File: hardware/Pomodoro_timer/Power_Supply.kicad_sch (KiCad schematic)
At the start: 17 parts, among them J1 USB_C_Receptacle_USB2.0_16P, J2 Battery_Terminals, Q1 FS8205A, U1 TP4056-42-ESOP8, U2 DW01A, U3 AP2127K-3.3

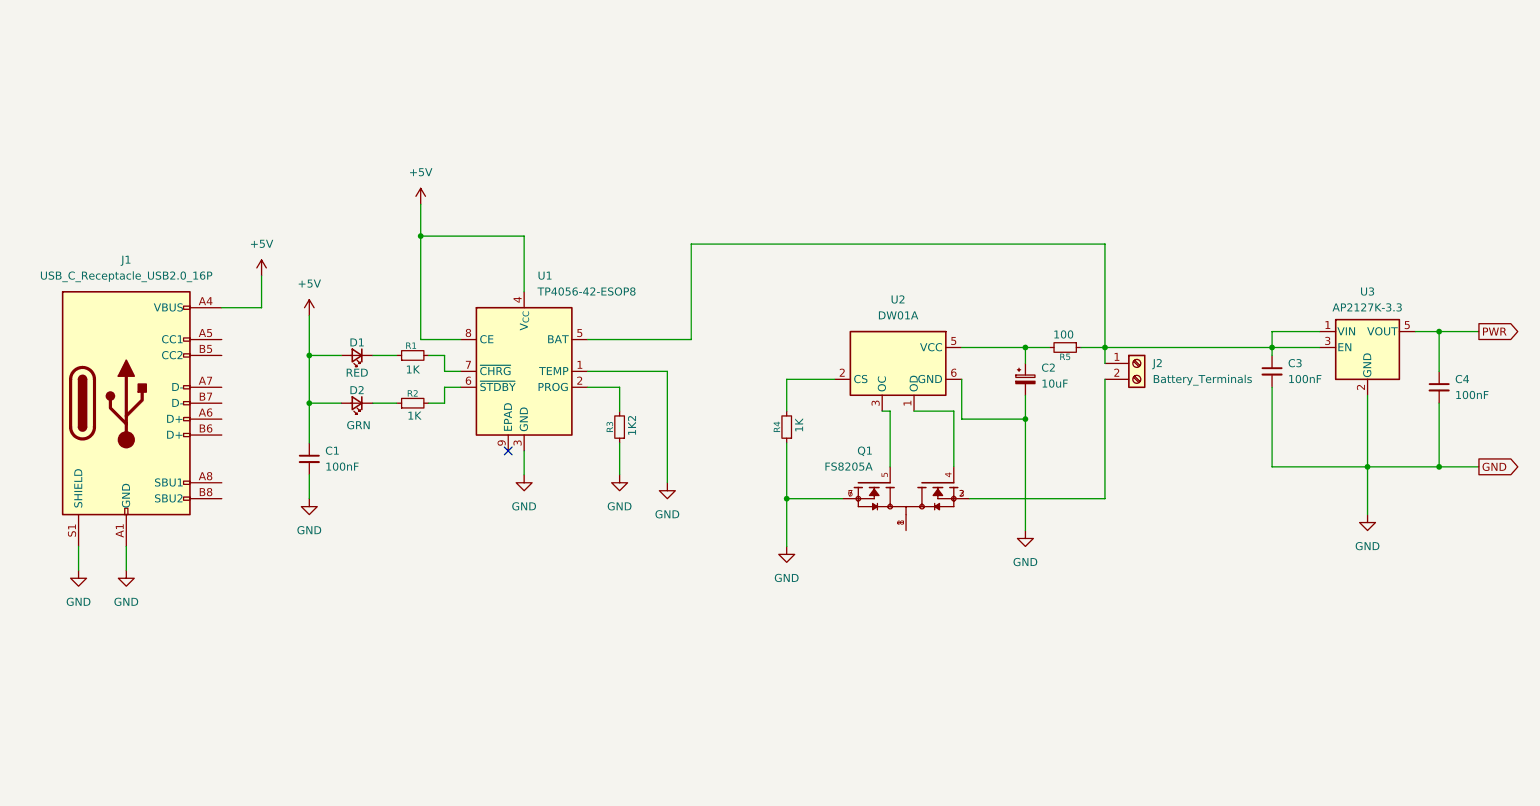
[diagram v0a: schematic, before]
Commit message: TM1637 Design started
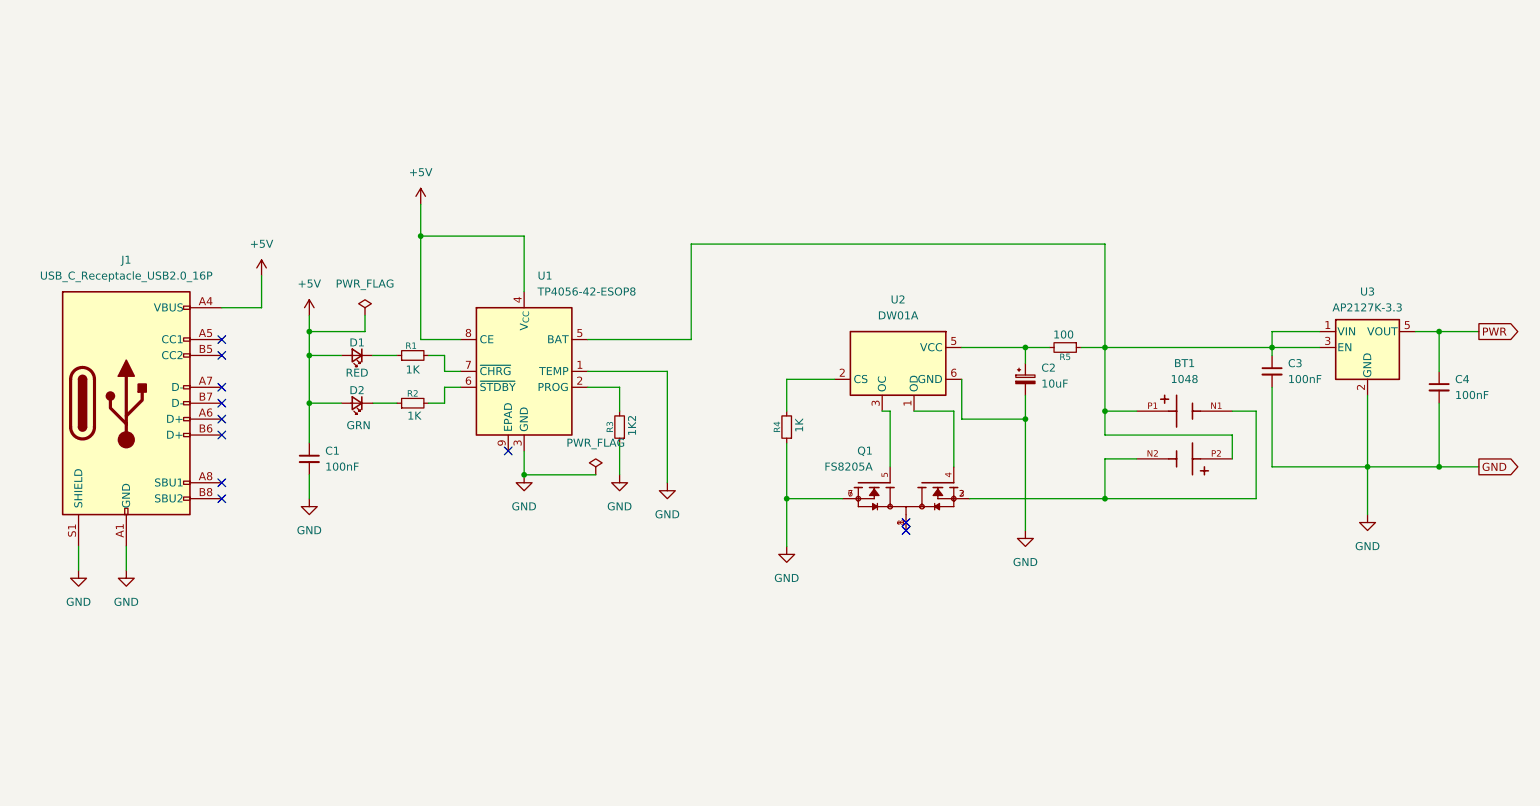
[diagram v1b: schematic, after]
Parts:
- removed J2: Battery_Terminals, symbol Connector:Screw_Terminal_01x02
- added BT1: 1048, 1048:BAT_1048, symbol 1048:1048
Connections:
- net at C3.1, R5.1, U1.5 (BAT)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: now also BT1.P1, BT1.P2
- net at Q1.2, Q1.3: now also BT1.N1, BT1.N2
- no-connect marks 1 -> 11

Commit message: PCB Ver.A : The Schematic completed the next part for PCB can be started.
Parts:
- removed BT1: 1048, 1048:BAT_1048, symbol 1048:1048
- removed C2: 10uF, symbol Device:C_Polarized_Small
- removed C3, C4: 100nF, symbol Device:C_Small
- removed D1: RED, symbol Device:LED_Small
- removed D2: GRN, symbol Device:LED_Small
- removed J1: USB_C_Receptacle_USB2.0_16P, symbol Connector:USB_C_Receptacle_USB2.0_16P
- removed Q1: FS8205A, FS8205A:SOP65P640X120-8N, symbol FS8205A:FS8205A
- removed R2, R4: 1K, symbol Device:R_Small
- removed R5: 100, symbol Device:R_Small
- removed U1: TP4056-42-ESOP8, Package_SO:SOIC-8-1EP_3.9x4.9mm_P1.27mm_EP2.41x3.3mm_ThermalVias, symbol Battery_Management:TP4056-42-ESOP8
- removed U2: DW01A, Package_TO_SOT_SMD:SOT-23-6, symbol Battery_Management:DW01A
- removed U3: AP2127K-3.3, Package_TO_SOT_SMD:SOT-223-3_TabPin2, symbol Regulator_Linear:AP2127K-3.3
- added BZ1: Buzzer, symbol Device:Buzzer
- added J1: Debug_Conn, symbol Connector:Conn_01x04_Pin
- added Q1: BC547, Package_TO_SOT_THT:TO-92, symbol Transistor_BJT:BC547
- added SW1: SW_Push, symbol Switch:SW_Push
- added U1: STM32G070CBTx, Package_QFP:LQFP-48_7x7mm_P0.5mm, symbol MCU_ST_STM32G0:STM32G070CBTx
- R3: value 1K2 -> 1K
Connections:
- net +5V is gone; now on net PWR: C1.1
- net GND: now also J1.1 (Pin_1), Q1.3 (E), SW1.1, U1.7 (VSS); no longer R3.1
- net PWR: now also R1.1, BZ1.1 (+), J1.4 (Pin_4), U1.4 (VBAT), U1.5 (VREF+), U1.6 (VDD)
- net at R3.2: now also Q1.2 (B)
- net at R1.2: now also SW1.2, U1.10 (NRST)
- new net: R3.1, U1.47 (PB8)
- new net: J1.2 (Pin_2), U1.36 (PA14)
- new net: J1.3 (Pin_3), U1.35 (PA13)
- new net: BZ1.2 (-), Q1.1 (C)
- new net CLK: U1.26 (PB14)
- new net DIO: U1.27 (PB15)
- no-connect marks 11 -> 0

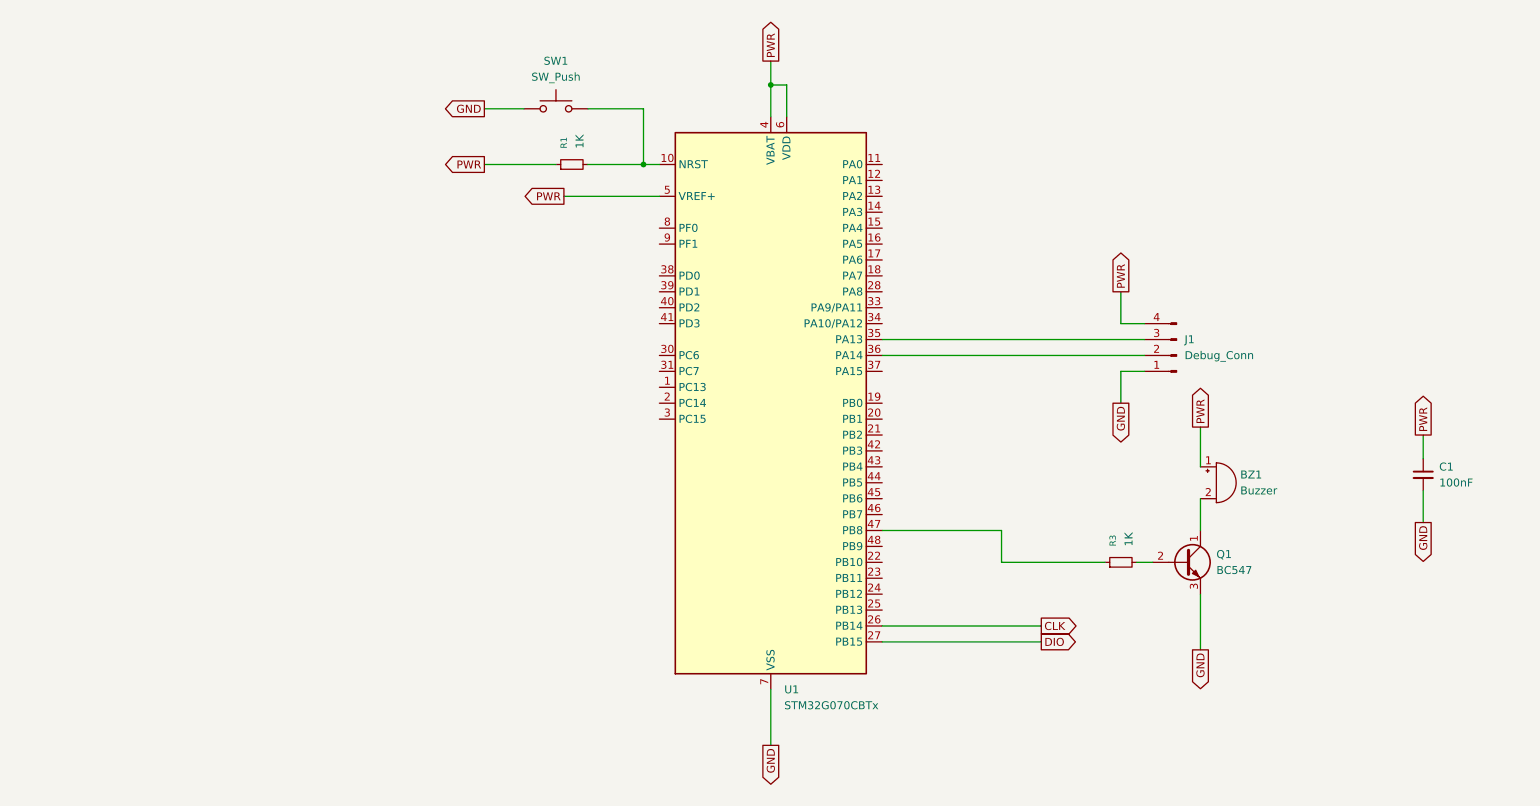
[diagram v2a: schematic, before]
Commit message: PCB Ver.A The required changes were not in line So made few alterations Need to start again
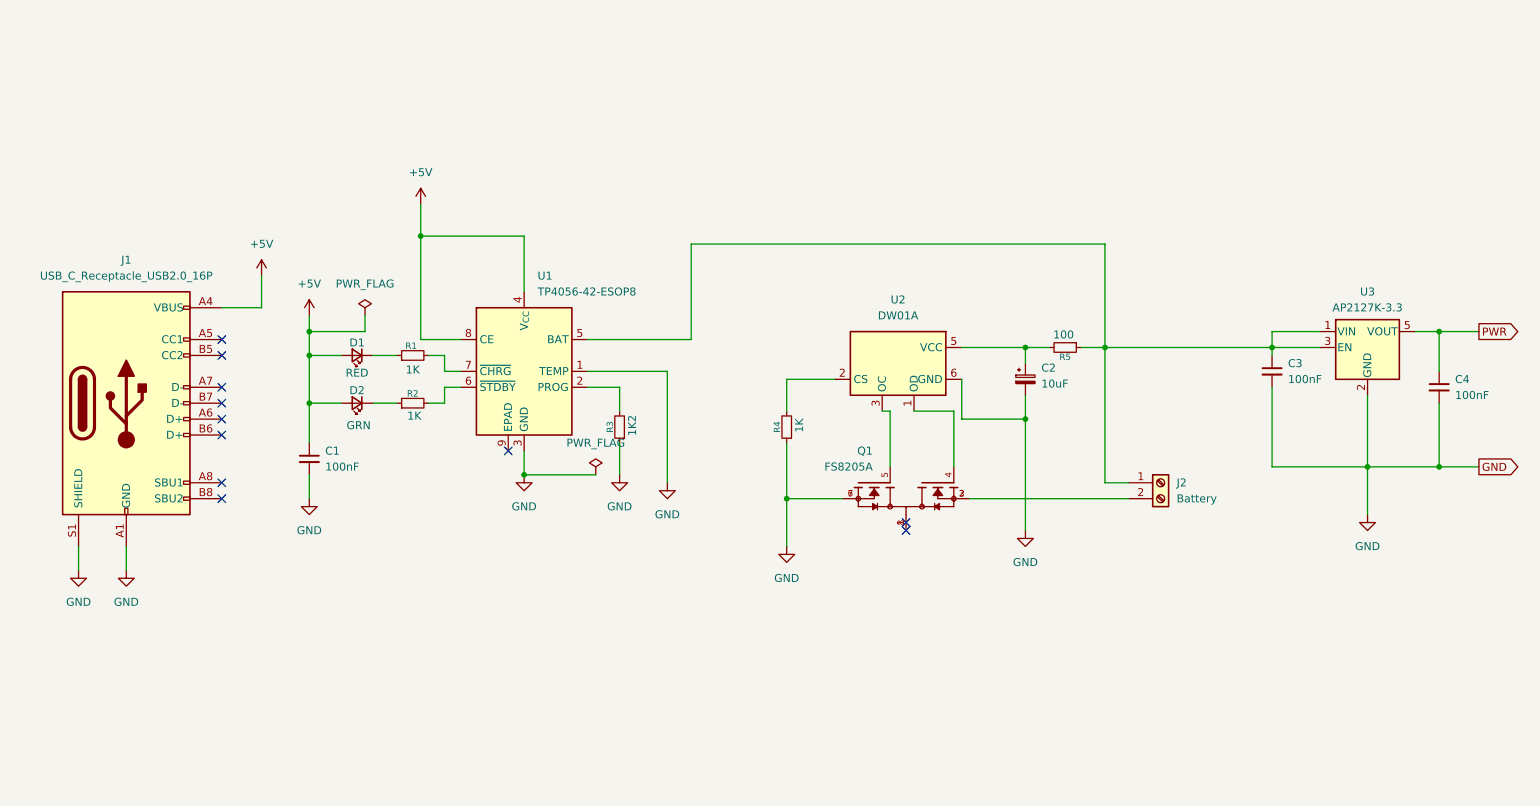
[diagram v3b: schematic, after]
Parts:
- removed BZ1: Buzzer, symbol Device:Buzzer
- removed J1: Debug_Conn, symbol Connector:Conn_01x04_Pin
- removed Q1: BC547, Package_TO_SOT_THT:TO-92, symbol Transistor_BJT:BC547
- removed SW1: SW_Push, symbol Switch:SW_Push
- removed U1: STM32G070CBTx, Package_QFP:LQFP-48_7x7mm_P0.5mm, symbol MCU_ST_STM32G0:STM32G070CBTx
- added C2: 10uF, symbol Device:C_Polarized_Small
- added C3, C4: 100nF, symbol Device:C_Small
- added D1: RED, symbol Device:LED_Small
- added D2: GRN, symbol Device:LED_Small
- added J1: USB_C_Receptacle_USB2.0_16P, symbol Connector:USB_C_Receptacle_USB2.0_16P
- added J2: Battery, symbol Connector:Screw_Terminal_01x02
- added Q1: FS8205A, FS8205A:SOP65P640X120-8N, symbol FS8205A:FS8205A
- added R2, R4: 1K, symbol Device:R_Small
- added R5: 100, symbol Device:R_Small
- added U1: TP4056-42-ESOP8, Package_SO:SOIC-8-1EP_3.9x4.9mm_P1.27mm_EP2.41x3.3mm_ThermalVias, symbol Battery_Management:TP4056-42-ESOP8
- added U2: DW01A, Package_TO_SOT_SMD:SOT-23-6, symbol Battery_Management:DW01A
- added U3: AP2127K-3.3, Package_TO_SOT_SMD:SOT-223-3_TabPin2, symbol Regulator_Linear:AP2127K-3.3
- R3: value 1K -> 1K2
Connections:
- net GND: now also R3.1, C2.2, C3.2, C4.2, J1.A1 (GND), J1.A12 (GND), J1.B1 (GND), J1.B12 (GND), J1.S1 (SHIELD), Q1.6, Q1.7, R4.1, U1.1 (TEMP), U1.3 (GND), U2.6 (GND), U3.2 (GND)
- net PWR: now also C4.1, U3.5 (VOUT); no longer C1.1, R1.1
- net at R3.2: now also U1.2 (PROG)
- net at R1.2: now also U1.7 (~{CHRG})
- new net: C3.1, J2.1 (Pin_1), R5.1, U1.5 (BAT), U3.1 (VIN), U3.3 (EN)
- new net: D2.1 (K), R2.1
- new net: R4.2, U2.2 (CS)
- new net: D1.1 (K), R1.1
- new net: Q1.1, Q1.8
- new net: J2.2 (Pin_2), Q1.2, Q1.3
- new net: Q1.4, U2.1 (OD)
- new net: Q1.5, U2.3 (OC)
- new net: C2.1, R5.2, U2.5 (VCC)
- new net: R2.2, U1.6 (~{STDBY})
- new net +5V: C1.1, D1.2 (A), D2.2 (A), J1.A4 (VBUS), J1.A9 (VBUS), J1.B4 (VBUS), J1.B9 (VBUS), U1.4 (V_{CC}), U1.8 (CE)
- no-connect marks 0 -> 11

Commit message: PCB Ver.A All changes finalized & PCB design has been started
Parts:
- removed J1: USB_C_Receptacle_USB2.0_16P, symbol Connector:USB_C_Receptacle_USB2.0_16P
- added J1: USB_C_Receptacle_PowerOnly_6P, Connector_USB:USB_C_Receptacle_GCT_USB4125-xx-x_6P_TopMnt_Horizontal, symbol Connector:USB_C_Receptacle_PowerOnly_6P
- added R1, R2: 5K1, Resistor_SMD:R_1206_3216Metric_Pad1.30x1.75mm_HandSolder, symbol Device:R_Small
- C1, C2, C3, C4: footprint (none) -> Capacitor_SMD:C_1206_3216Metric_Pad1.33x1.80mm_HandSolder
- D1, D2: footprint (none) -> LED_SMD:LED_1206_3216Metric_Pad1.42x1.75mm_HandSolder
- J2: footprint (none) -> Connector_PinHeader_2.54mm:PinHeader_1x02_P2.54mm_Vertical
- Q1: footprint FS8205A:SOP65P640X120-8N -> SOP65P640X120:SOP65P640X120-8N
- R3: renamed from R1; footprint (none) -> Resistor_SMD:R_1206_3216Metric_Pad1.30x1.75mm_HandSolder
- R4: renamed from R2; footprint (none) -> Resistor_SMD:R_1206_3216Metric_Pad1.30x1.75mm_HandSolder
- R5: renamed from R3; footprint (none) -> Resistor_SMD:R_1206_3216Metric_Pad1.30x1.75mm_HandSolder
- R6: renamed from R4; footprint (none) -> Resistor_SMD:R_1206_3216Metric_Pad1.30x1.75mm_HandSolder
- R7: renamed from R5; footprint (none) -> Resistor_SMD:R_1206_3216Metric_Pad1.30x1.75mm_HandSolder
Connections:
- net +5V: now also J1.A9 (VBUS), J1.B9 (VBUS)
- net GND: now also J1.A12 (GND), J1.B12 (GND), J1.S1 (SHIELD), R1.1, R2.1
- new net: J1.A5 (CC1), R2.2
- new net: J1.B5 (CC2), R1.2
- no-connect marks 11 -> 2
